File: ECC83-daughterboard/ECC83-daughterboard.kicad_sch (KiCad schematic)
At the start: 20 parts, among them Q1 IRF7495, T2 EP7_750310020, U1 LM5156HPWP, U2 ECC83

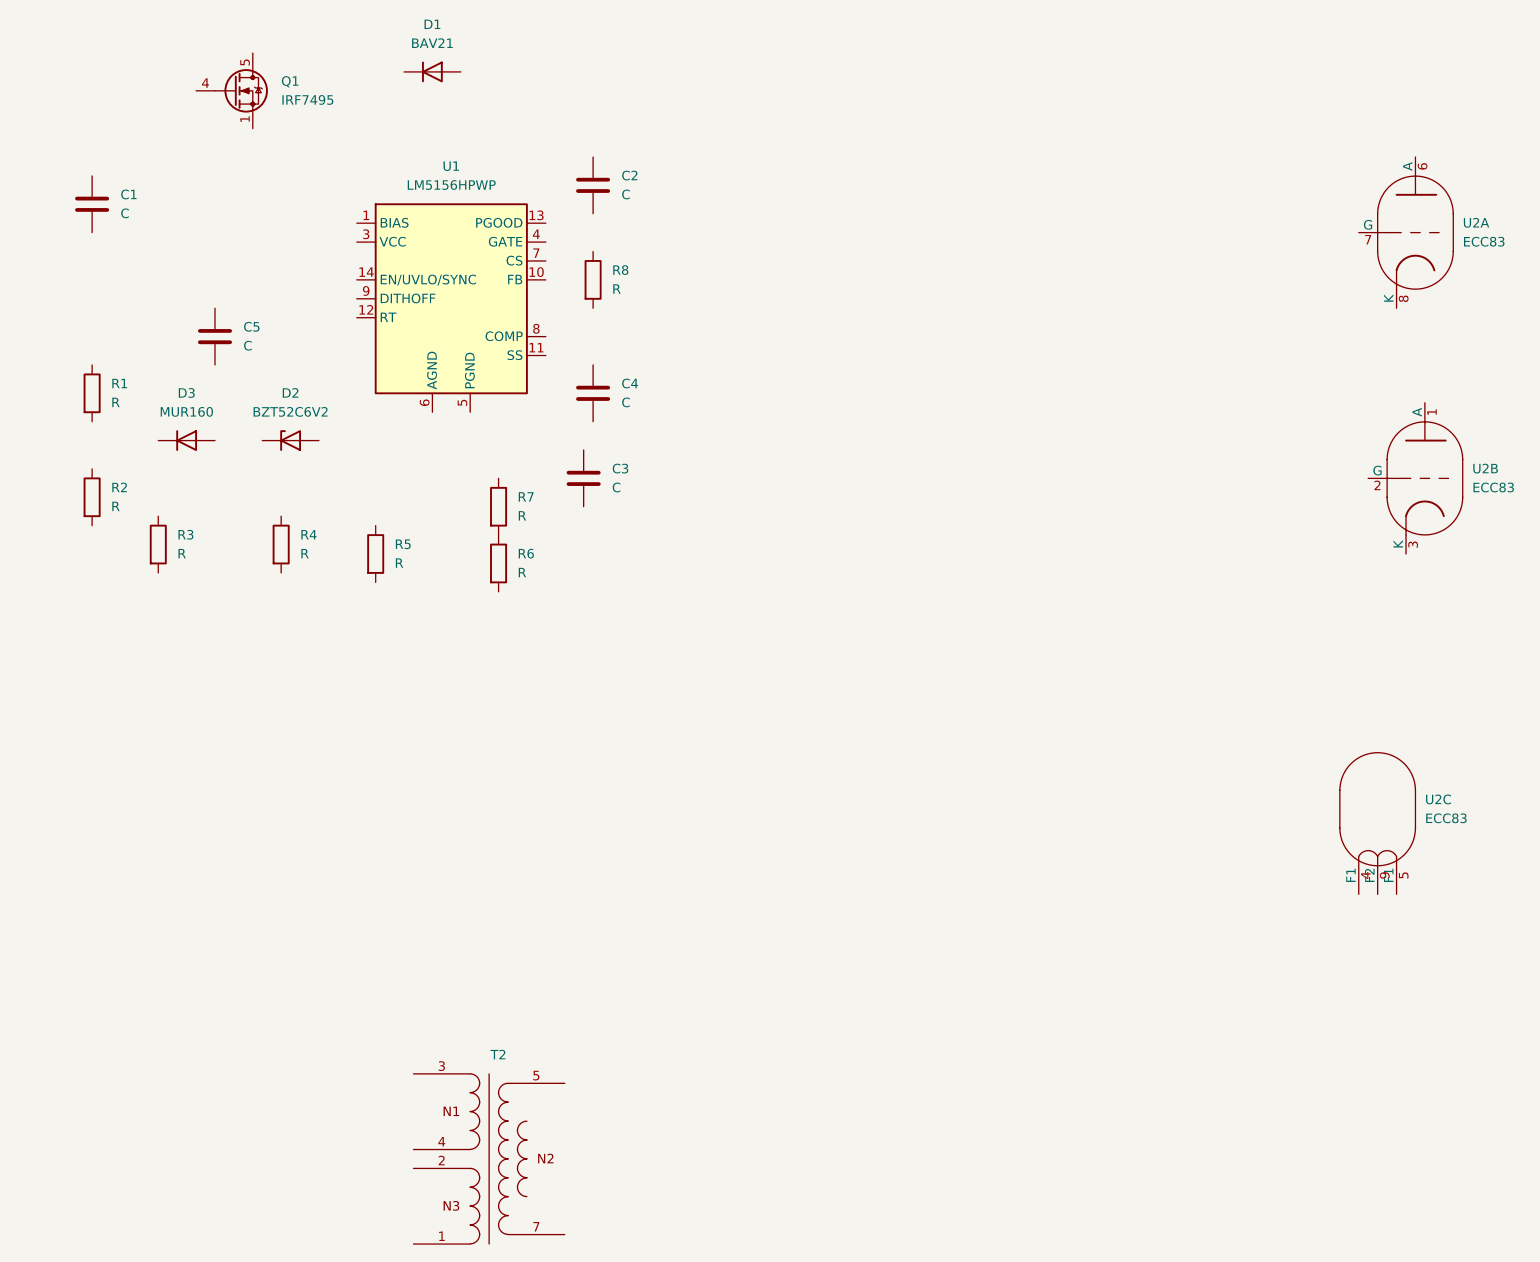
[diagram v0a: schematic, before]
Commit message: moved stuff to correct schematics, decided on a HV controller
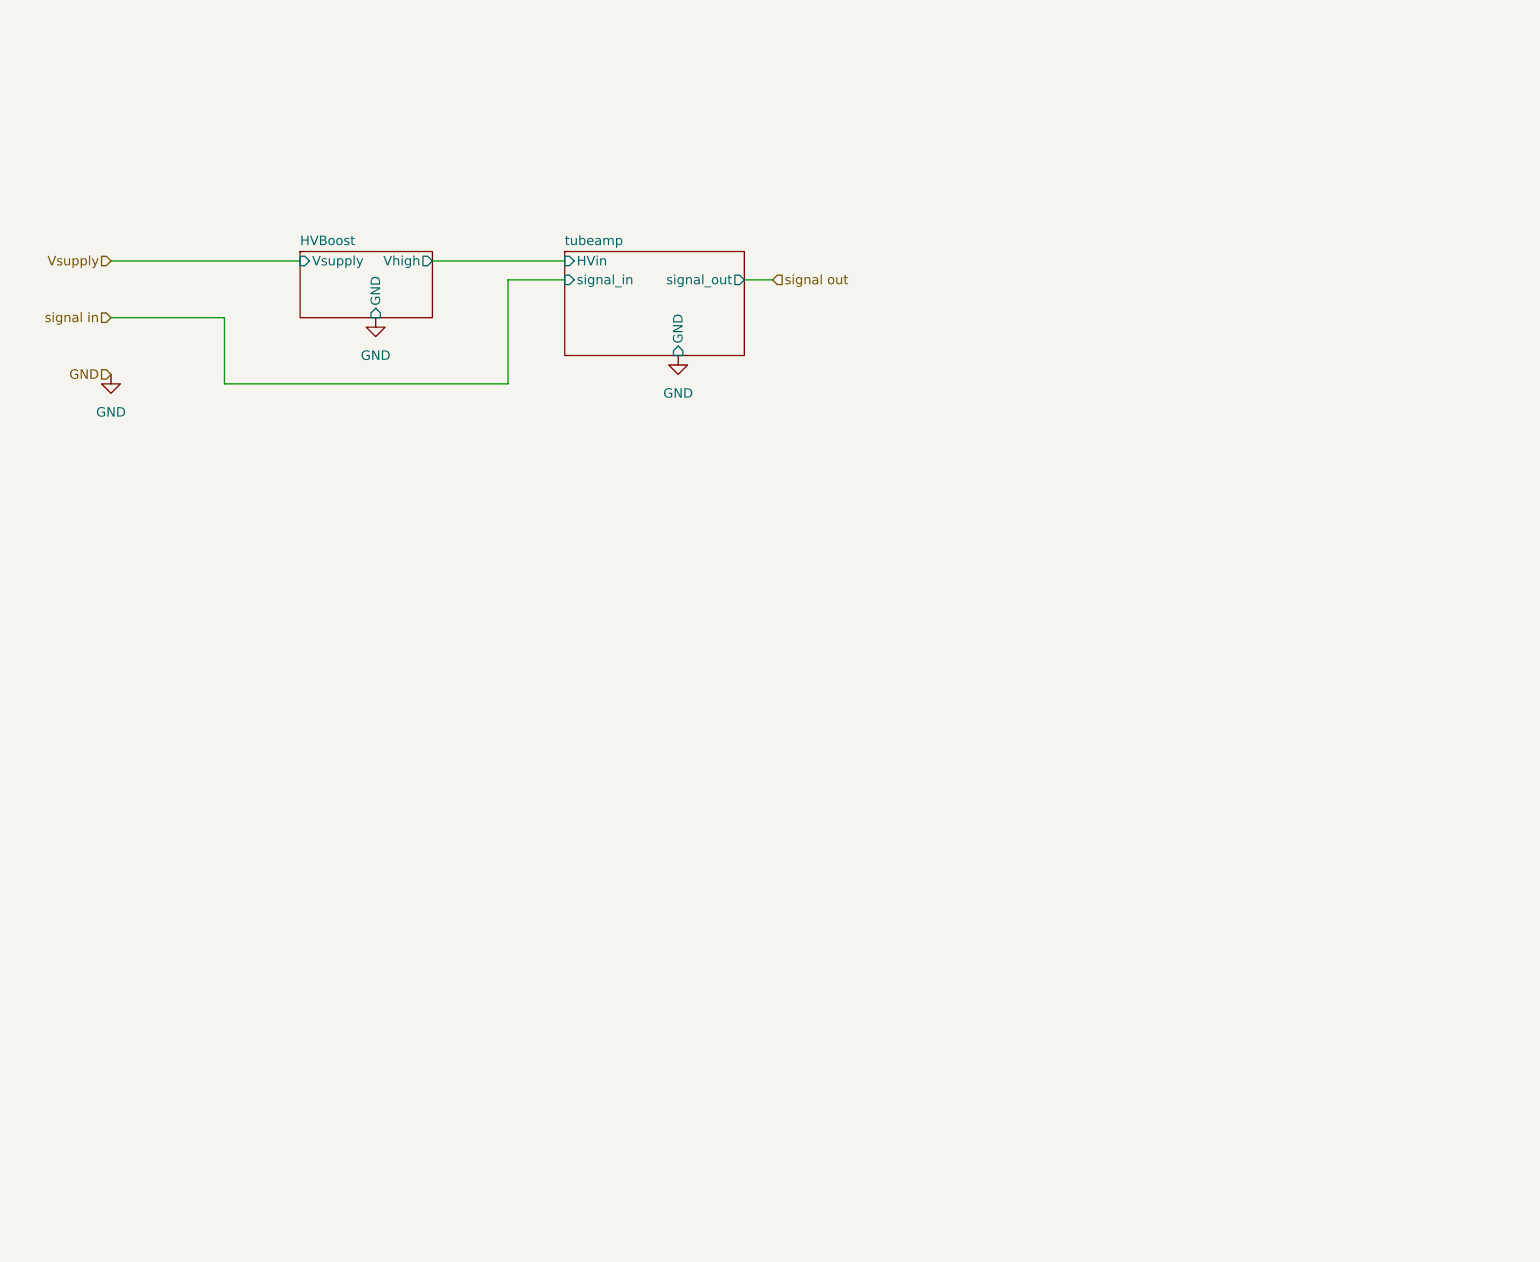
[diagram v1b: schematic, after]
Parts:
- removed C1, C2, C3, C4, C5: C, Capacitor_SMD:C_0603_1608Metric_Pad1.08x0.95mm_HandSolder, symbol Device:C
- removed D1: BAV21, Diode_THT:D_DO-35_SOD27_P7.62mm_Horizontal, symbol Diode:BAV21
- removed D2: BZT52C6V2, Diode_SMD:D_SOD-123F, symbol Diode:BZT52Bxx
- removed D3: MUR160, Diode_THT:D_DO-41_SOD81_P10.16mm_Horizontal, symbol Diode:1N4001
- removed Q1: IRF7495, Package_SO:SOIC-8_3.9x4.9mm_P1.27mm, symbol Transistor_FET:IRF7403
- removed R1, R2, R3, R4, R5, R6, R7, R8: R, Resistor_SMD:R_0402_1005Metric_Pad0.72x0.64mm_HandSolder, symbol Device:R
- removed T2: EP7_750310020, WE-PoE:T_Wurth_WE-PoE-EP7, symbol WE-PoE:EP7_750310020
- removed U1: LM5156HPWP, Package_SO:Texas_HTSSOP-14-1EP_4.4x5mm_P0.65mm_EP3.4x5mm_Mask3.155x3.255mm_ThermalVias, symbol Regulator_Switching:LM5156HPWP
- removed U2: ECC83, Valve:Valve_Noval_P, symbol Valve:ECC83
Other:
- added sheet HVBoost (HVBoost.kicad_sch)
- added sheet tubeamp (tubeamp.kicad_sch)

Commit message: HV boost schematic in line with datasheet, half-calculated values
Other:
- company: (none) -> nacho.works
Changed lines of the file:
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@@
 	(generator_version "9.0")
 	(paper "A4")
+	(title_block
+		(date "2026-04-20")
+		(company "nacho.works")
+	)
 	(wire
 		(pts
@@
 		(dnp no)
 		(fields_autoplaced yes)
-		(property "Reference" "#PWR013"
+		(property "Reference" "#PWR02"
 			(at 82.55 74.93 0)
 			(effects
@@
 			(project "ECC83-daughterboard"
 				(path "/6631e6c4-daf1-4ebd-bf40-608d44fc040a"
-					(reference "#PWR013")
+					(reference "#PWR02")
 					(unit 1)
 				)
@@
 		(dnp no)
 		(fields_autoplaced yes)
-		(property "Reference" "#PWR012"
+		(property "Reference" "#PWR01"
 			(at 46.99 82.55 0)
 			(effects
@@
 		)
 		(instances
-			(project ""
+			(project "ECC83-daughterboard"
 				(path "/6631e6c4-daf1-4ebd-bf40-608d44fc040a"
-					(reference "#PWR012")
+					(reference "#PWR01")
 					(unit 1)
 				)
@@
 		(dnp no)
 		(fields_autoplaced yes)
-		(property "Reference" "#PWR014"
+		(property "Reference" "#PWR03"
 			(at 123.19 80.01 0)
 			(effects
@@
 			(project "ECC83-daughterboard"
 				(path "/6631e6c4-daf1-4ebd-bf40-608d44fc040a"
-					(reference "#PWR014")
+					(reference "#PWR03")
 					(unit 1)
 				)
